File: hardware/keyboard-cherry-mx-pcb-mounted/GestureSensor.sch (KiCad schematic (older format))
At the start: 21 parts, among them U2 PCA9546AD, U3 APDS-9960, U4 APDS-9960, U7 APDS-9960, U8 APDS-9960

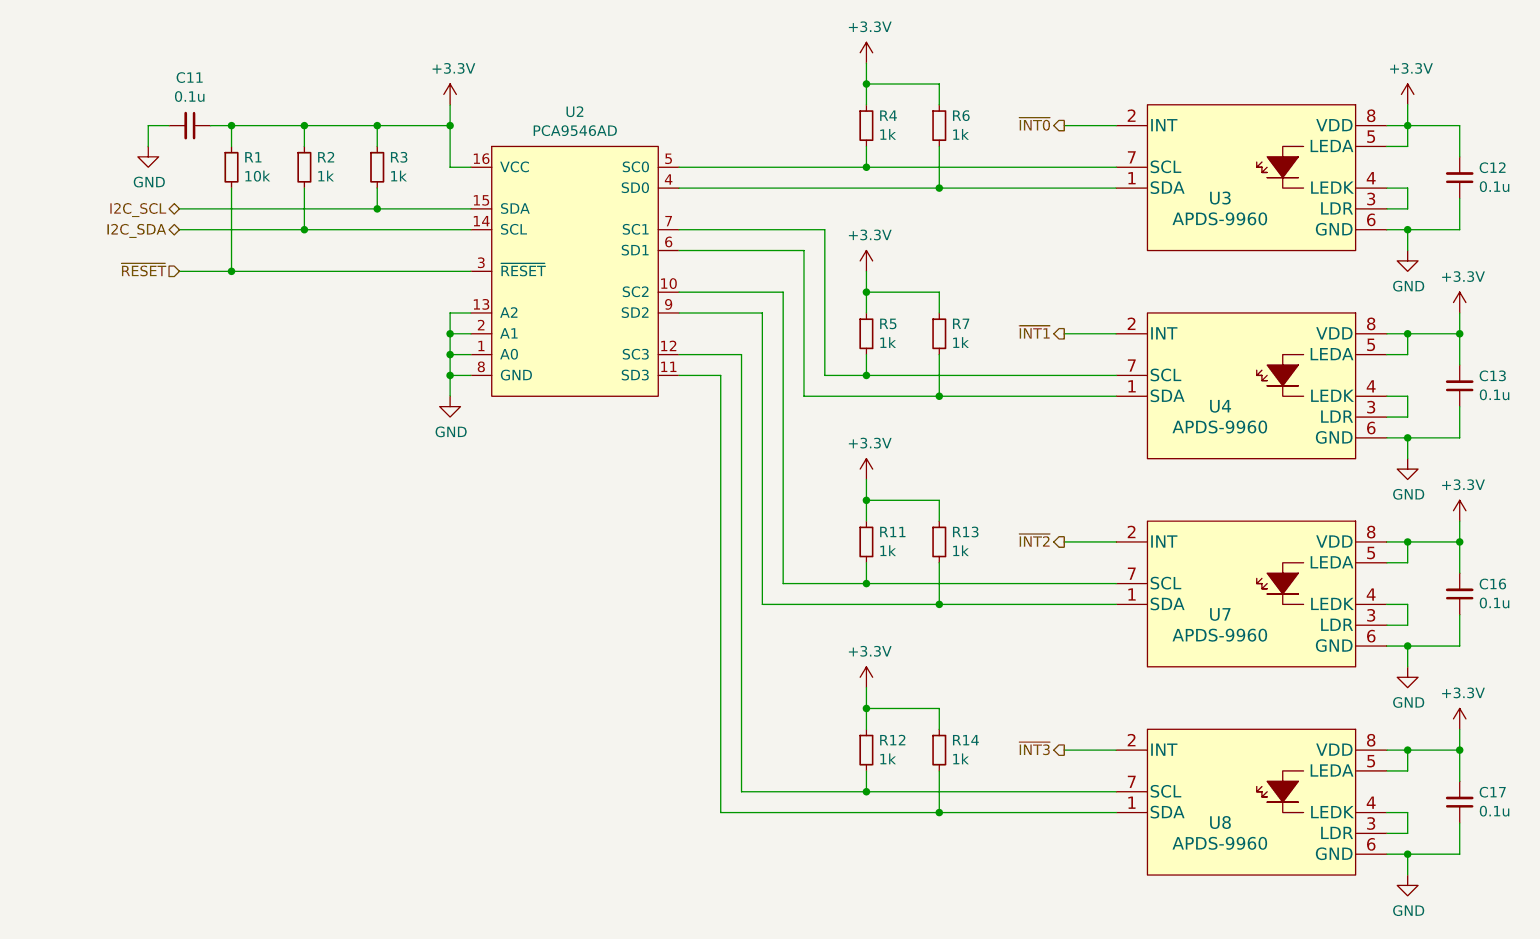
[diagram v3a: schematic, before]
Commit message: Aligns the keys so the column connections are more consistent. e.g. right most keys will have same column connection.
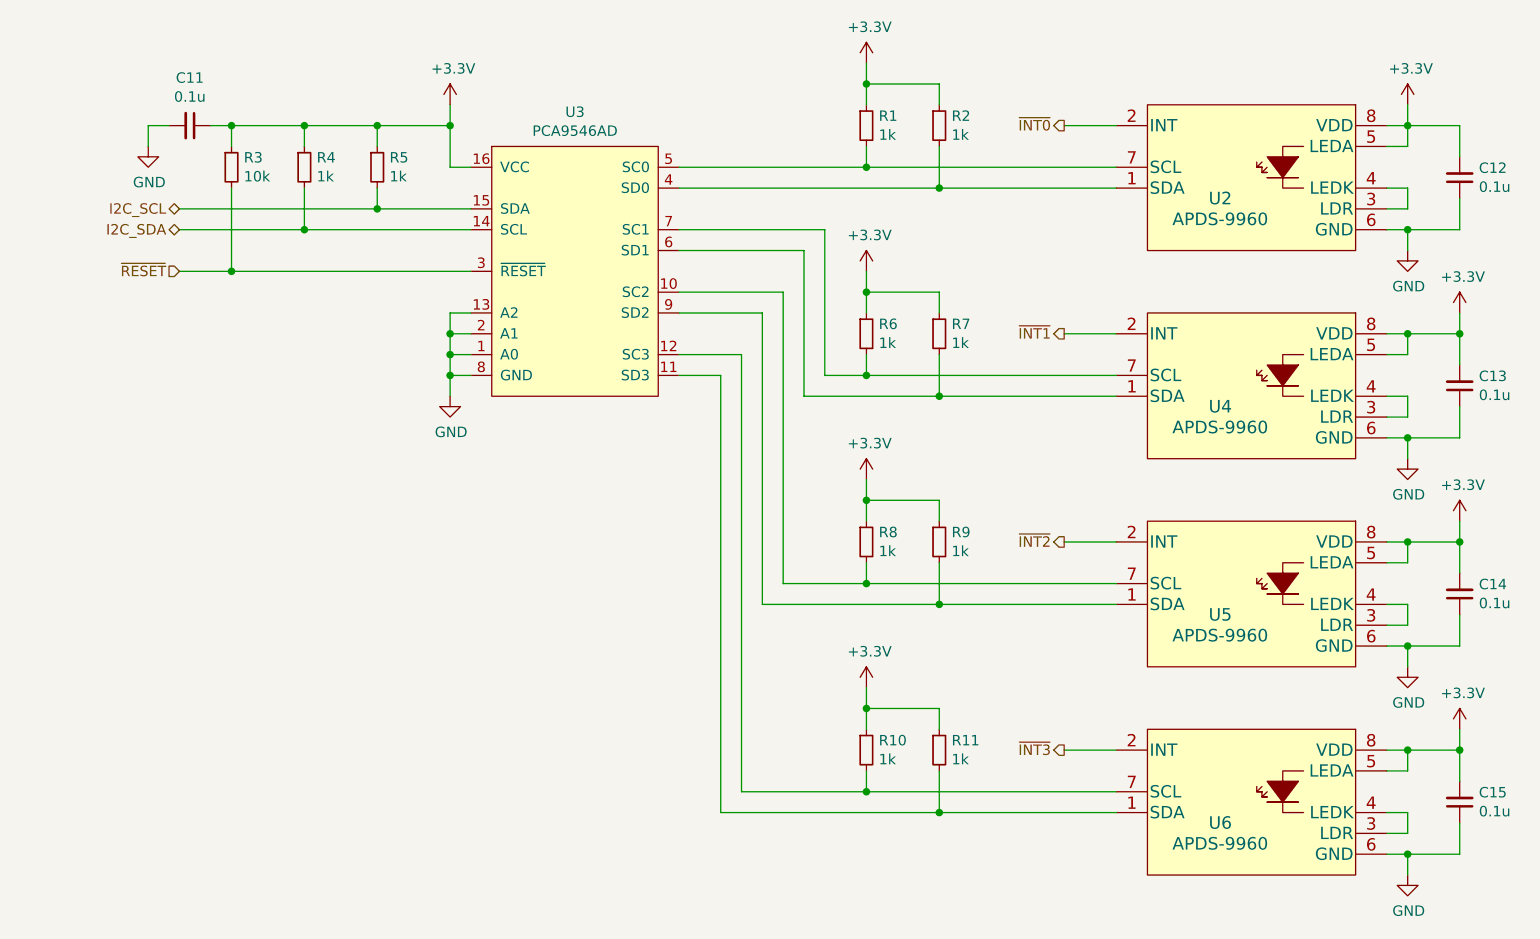
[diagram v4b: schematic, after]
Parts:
- renumbered C16 to C14, C17 to C15, R4 to R1, R12 to R10, R14 to R11, R6 to R2, R1 to R3, R2 to R4, R3 to R5, R5 to R6, R11 to R8, R13 to R9, U3 to U2, U2 to U3, U7 to U5, U8 to U6
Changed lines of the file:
@@
 $EndDescr
 $Comp
-L Sij_Sensors:APDS-9930 U3
+L Sij_Sensors:APDS-9930 U2
 U 1 1 5E817D7C
 P 7550 1300
-F 0 "U3" H 7700 850 60  0000 C CNN
+F 0 "U2" H 7700 850 60  0000 C CNN
 F 1 "APDS-9960" H 7700 750 60  0000 C CNN
 F 2 "Sij_Sensors:APDS-9930" H 8350 1540 60  0001 C CNN
@@
 $EndComp
 $Comp
-L power:+3.3V #PWR015
+L power:+3.3V #PWR014
 U 1 1 5E836120
 P 5700 1100
-F 0 "#PWR015" H 5700 950 50  0001 C CNN
+F 0 "#PWR014" H 5700 950 50  0001 C CNN
 F 1 "+3.3V" H 5715 1273 50  0000 C CNN
 F 2 "" H 5700 1100 50  0001 C CNN
@@
 	6650 2400 6900 2400
 $Comp
-L Device:R_Small R5
+L Device:R_Small R6
 U 1 1 5E84F8D3
 P 5700 2400
-F 0 "R5" H 5759 2446 50  0000 L CNN
+F 0 "R6" H 5759 2446 50  0000 L CNN
 F 1 "1k" H 5759 2355 50  0000 L CNN
 F 2 "Resistor_SMD:R_0805_2012Metric" H 5700 2400 50  0001 C CNN
@@
 $EndComp
 $Comp
-L power:+3.3V #PWR016
+L power:+3.3V #PWR019
 U 1 1 5E84F8D9
 P 5700 2100
-F 0 "#PWR016" H 5700 1950 50  0001 C CNN
+F 0 "#PWR019" H 5700 1950 50  0001 C CNN
 F 1 "+3.3V" H 5715 2273 50  0000 C CNN
 F 2 "" H 5700 2100 50  0001 C CNN
@@
 	6050 1300 6050 1200
 $Comp
-L Device:R_Small R6
+L Device:R_Small R2
 U 1 1 5E839151
 P 6050 1400
-F 0 "R6" H 6109 1446 50  0000 L CNN
+F 0 "R2" H 6109 1446 50  0000 L CNN
 F 1 "1k" H 6109 1355 50  0000 L CNN
 F 2 "Resistor_SMD:R_0805_2012Metric" H 6050 1400 50  0001 C CNN
@@
 	5700 1600 5700 1500
 $Comp
-L Device:R_Small R4
+L Device:R_Small R1
 U 1 1 5E832D68
 P 5700 1400
-F 0 "R4" H 5759 1446 50  0000 L CNN
+F 0 "R1" H 5759 1446 50  0000 L CNN
 F 1 "1k" H 5759 1355 50  0000 L CNN
 F 2 "Resistor_SMD:R_0805_2012Metric" H 5700 1400 50  0001 C CNN
@@
 	8300 1900 8300 2000
 $Comp
-L power:GND #PWR019
+L power:GND #PWR022
 U 1 1 5E8694B6
 P 8300 3000
-F 0 "#PWR019" H 8300 2750 50  0001 C CNN
+F 0 "#PWR022" H 8300 2750 50  0001 C CNN
 F 1 "GND" H 8305 2827 50  0000 C CNN
 F 2 "" H 8300 3000 50  0001 C CNN
@@
 	8300 2900 8300 3000
 $Comp
-L power:+3.3V #PWR017
+L power:+3.3V #PWR016
 U 1 1 5E86B9E5
 P 8300 1300
-F 0 "#PWR017" H 8300 1150 50  0001 C CNN
+F 0 "#PWR016" H 8300 1150 50  0001 C CNN
 F 1 "+3.3V" H 8315 1473 50  0000 C CNN
 F 2 "" H 8300 1300 50  0001 C CNN
@@
 	2250 1500 2250 1400
 $Comp
-L power:GND #PWR012
+L power:GND #PWR017
 U 1 1 5E834566
 P 2250 1500
-F 0 "#PWR012" H 2250 1250 50  0001 C CNN
+F 0 "#PWR017" H 2250 1250 50  0001 C CNN
 F 1 "GND" H 2255 1327 50  0000 C CNN
 F 2 "" H 2250 1500 50  0001 C CNN
@@
 	3700 1400 3350 1400
 $Comp
-L Device:R_Small R3
+L Device:R_Small R5
 U 1 1 5E82D8BA
 P 3350 1600
-F 0 "R3" H 3409 1646 50  0000 L CNN
+F 0 "R5" H 3409 1646 50  0000 L CNN
 F 1 "1k" H 3409 1555 50  0000 L CNN
 F 2 "Resistor_SMD:R_0805_2012Metric" H 3350 1600 50  0001 C CNN
@@
 $EndComp
 $Comp
-L Device:R_Small R2
+L Device:R_Small R4
 U 1 1 5E82D111
 P 3000 1600
-F 0 "R2" H 3059 1646 50  0000 L CNN
+F 0 "R4" H 3059 1646 50  0000 L CNN
 F 1 "1k" H 3059 1555 50  0000 L CNN
 F 2 "Resistor_SMD:R_0805_2012Metric" H 3000 1600 50  0001 C CNN
@@
 $EndComp
 $Comp
-L Device:R_Small R1
+L Device:R_Small R3
 U 1 1 5E82BA93
 P 2650 1600
-F 0 "R1" H 2709 1646 50  0000 L CNN
+F 0 "R3" H 2709 1646 50  0000 L CNN
 F 1 "10k" H 2709 1555 50  0000 L CNN
 F 2 "Resistor_SMD:R_0805_2012Metric" H 2650 1600 50  0001 C CNN
@@
 	3700 1300 3700 1400
 $Comp
-L power:+3.3V #PWR013
+L power:+3.3V #PWR015
 U 1 1 5E82ABAB
 P 3700 1300
-F 0 "#PWR013" H 3700 1150 50  0001 C CNN
+F 0 "#PWR015" H 3700 1150 50  0001 C CNN
 F 1 "+3.3V" H 3715 1473 50  0000 C CNN
 F 2 "" H 3700 1300 50  0001 C CNN
@@
 $EndComp
 $Comp
-L power:GND #PWR014
+L power:GND #PWR021
 U 1 1 5E826F2D
 P 3700 2700
-F 0 "#PWR014" H 3700 2450 50  0001 C CNN
+F 0 "#PWR021" H 3700 2450 50  0001 C CNN
 F 1 "GND" H 3705 2527 50  0000 C CNN
 F 2 "" H 3700 2700 50  0001 C CNN
@@
 	3800 2500 3700 2500
 $Comp
-L Sij_MUX:PCA9546AD U2
+L Sij_MUX:PCA9546AD U3
 U 1 1 5E782AA5
 P 4300 1500
-F 0 "U2" H 4300 1665 50  0000 C CNN
+F 0 "U3" H 4300 1665 50  0000 C CNN
 F 1 "PCA9546AD" H 4300 1574 50  0000 C CNN
 F 2 "Package_SO:SOIC-16_3.9x9.9mm_P1.27mm" H 4300 1500 50  0001 C CNN
@@
 Connection ~ 3700 2400
 $Comp
-L Sij_Sensors:APDS-9930 U7
+L Sij_Sensors:APDS-9930 U5
 U 1 1 5E7B0BE0
 P 7550 3300
-F 0 "U7" H 7700 2850 60  0000 C CNN
+F 0 "U5" H 7700 2850 60  0000 C CNN
 F 1 "APDS-9960" H 7700 2750 60  0000 C CNN
 F 2 "Sij_Sensors:APDS-9930" H 8350 3540 60  0001 C CNN
@@
 $EndComp
 $Comp
-L Sij_Sensors:APDS-9930 U8
+L Sij_Sensors:APDS-9930 U6
 U 1 1 5E7B0BE6
 P 7550 4300
-F 0 "U8" H 7700 3850 60  0000 C CNN
+F 0 "U6" H 7700 3850 60  0000 C CNN
 F 1 "APDS-9960" H 7700 3750 60  0000 C CNN
 F 2 "Sij_Sensors:APDS-9930" H 8350 4540 60  0001 C CNN
@@
 $EndComp
 $Comp
-L power:+3.3V #PWR025
+L power:+3.3V #PWR023
 U 1 1 5E7B0BEC
 P 5700 3100
-F 0 "#PWR025" H 5700 2950 50  0001 C CNN
+F 0 "#PWR023" H 5700 2950 50  0001 C CNN
 F 1 "+3.3V" H 5715 3273 50  0000 C CNN
 F 2 "" H 5700 3100 50  0001 C CNN
@@
 	6650 4400 6900 4400
 $Comp
-L Device:R_Small R12
+L Device:R_Small R10
 U 1 1 5E7B0BF6
 P 5700 4400
-F 0 "R12" H 5759 4446 50  0000 L CNN
+F 0 "R10" H 5759 4446 50  0000 L CNN
 F 1 "1k" H 5759 4355 50  0000 L CNN
 F 2 "Resistor_SMD:R_0805_2012Metric" H 5700 4400 50  0001 C CNN
@@
 	5700 4300 5700 4200
 $Comp
-L Device:R_Small R14
+L Device:R_Small R11
 U 1 1 5E7B0C04
 P 6050 4400
-F 0 "R14" H 6109 4446 50  0000 L CNN
+F 0 "R11" H 6109 4446 50  0000 L CNN
 F 1 "1k" H 6109 4355 50  0000 L CNN
 F 2 "Resistor_SMD:R_0805_2012Metric" H 6050 4400 50  0001 C CNN
@@
 	6050 3300 6050 3200
 $Comp
-L Device:R_Small R13
+L Device:R_Small R9
 U 1 1 5E7B0C14
 P 6050 3400
-F 0 "R13" H 6109 3446 50  0000 L CNN
+F 0 "R9" H 6109 3446 50  0000 L CNN
 F 1 "1k" H 6109 3355 50  0000 L CNN
 F 2 "Resistor_SMD:R_0805_2012Metric" H 6050 3400 50  0001 C CNN
@@
 	5700 3600 5700 3500
 $Comp
-L Device:R_Small R11
+L Device:R_Small R8
 U 1 1 5E7B0C1C
 P 5700 3400
-F 0 "R11" H 5759 3446 50  0000 L CNN
+F 0 "R8" H 5759 3446 50  0000 L CNN
 F 1 "1k" H 5759 3355 50  0000 L CNN
 F 2 "Resistor_SMD:R_0805_2012Metric" H 5700 3400 50  0001 C CNN
@@
 	6050 4700 6900 4700
 $Comp
-L power:GND #PWR027
+L power:GND #PWR025
 U 1 1 5E7B0C26
 P 8300 4000
-F 0 "#PWR027" H 8300 3750 50  0001 C CNN
+F 0 "#PWR025" H 8300 3750 50  0001 C CNN
 F 1 "GND" H 8305 3827 50  0000 C CNN
 F 2 "" H 8300 4000 50  0001 C CNN
@@
 	8300 4900 8300 5000
 $Comp
-L power:+3.3V #PWR029
+L power:+3.3V #PWR024
 U 1 1 5E7B0C3C
 P 8550 3300
-F 0 "#PWR029" H 8550 3150 50  0001 C CNN
+F 0 "#PWR024" H 8550 3150 50  0001 C CNN
 F 1 "+3.3V" H 8565 3473 50  0000 C CNN
 F 2 "" H 8550 3300 50  0001 C CNN
@@
 Connection ~ 8300 3400
 $Comp
-L power:+3.3V #PWR030
+L power:+3.3V #PWR027
 U 1 1 5E7B0C47
 P 8550 4300
-F 0 "#PWR030" H 8550 4150 50  0001 C CNN
+F 0 "#PWR027" H 8550 4150 50  0001 C CNN
 F 1 "+3.3V" H 8565 4473 50  0000 C CNN
 F 2 "" H 8550 4300 50  0001 C CNN
@@
 	8300 4400 8550 4400
 $Comp
-L Device:C_Small C17
+L Device:C_Small C15
 U 1 1 5E7B0C53
 P 8550 4650
-F 0 "C17" H 8458 4604 50  0000 R CNN
+F 0 "C15" H 8458 4604 50  0000 R CNN
 F 1 "0.1u" H 8458 4695 50  0000 R CNN
 F 2 "Capacitor_SMD:C_0805_2012Metric" H 8550 4650 50  0001 C CNN
@@
 Connection ~ 8300 4900
 $Comp
-L Device:C_Small C16
+L Device:C_Small C14
 U 1 1 5E7B0C5E
 P 8550 3650
-F 0 "C16" H 8458 3604 50  0000 R CNN
+F 0 "C14" H 8458 3604 50  0000 R CNN
 F 1 "0.1u" H 8458 3695 50  0000 R CNN
 F 2 "Capacitor_SMD:C_0805_2012Metric" H 8550 3650 50  0001 C CNN
